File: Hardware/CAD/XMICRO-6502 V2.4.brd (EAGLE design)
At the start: 203.2 x 101.6 mm, 80 parts, among them Q1 2N4403, U1 74138, U10 7474, U11 74273, U12 74244, U13 74244, U14 74244, U15 74245, U16 74574, U17 7400, U18 7408, U19 7404, U2 74138, U20 W65C02S, U21 74244, U22 74138, U23 74148, U24 74244, U25 74244, U26 74273, U27 7432, U28 7432, U29 74257, U3 7400, U30 7474, U31 74LS14N, U4 7404, U5 74257, U6 74688, U7 74688, U8 74244, U9 7474, Y1 4MHz

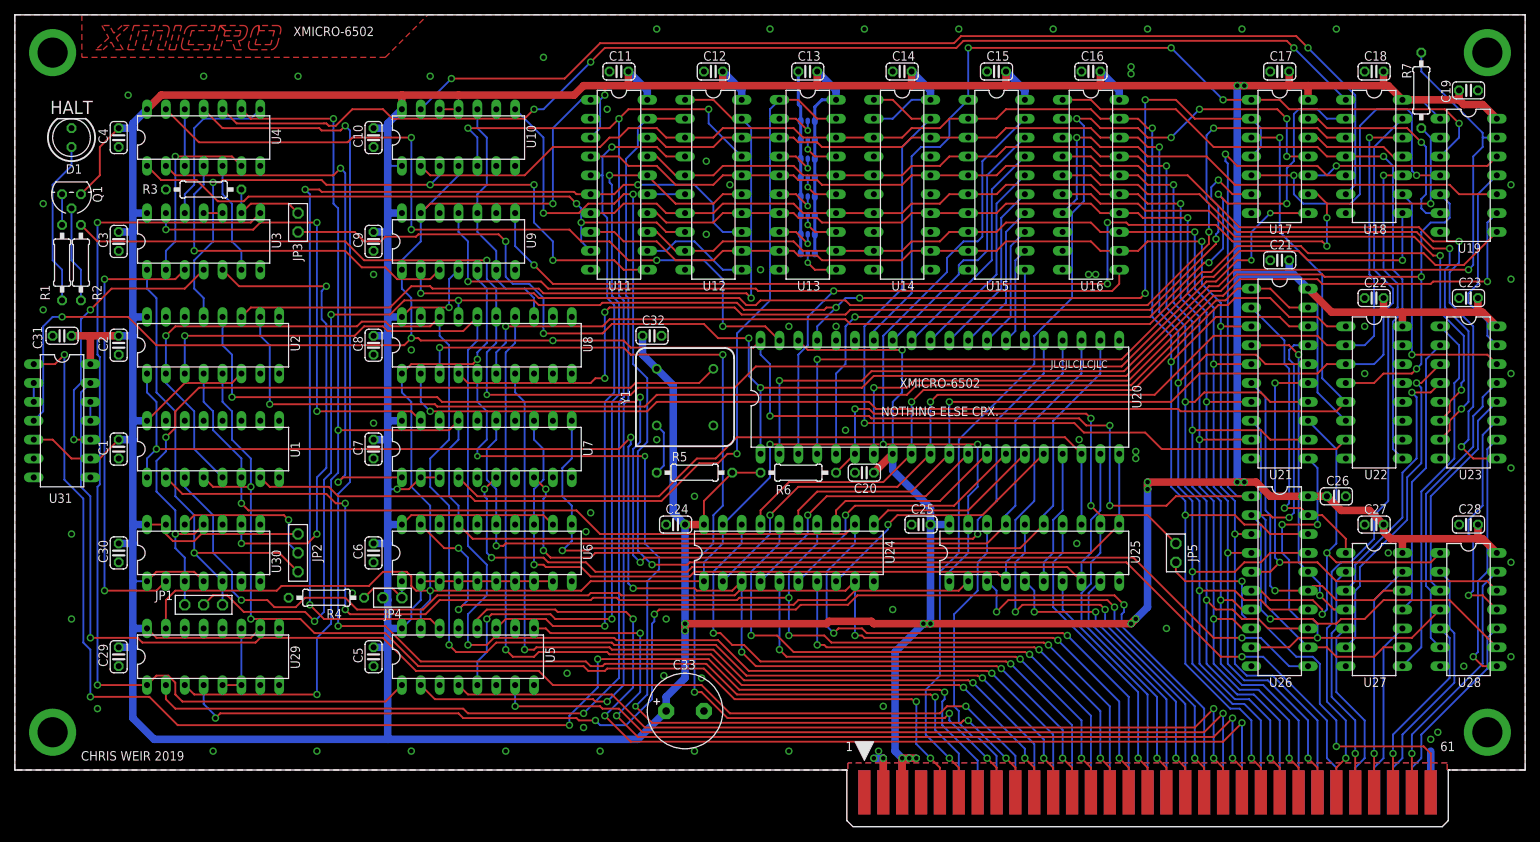
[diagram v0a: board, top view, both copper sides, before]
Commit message: Updated to V2.4 - made it necessary to manually clear DMA interrupts
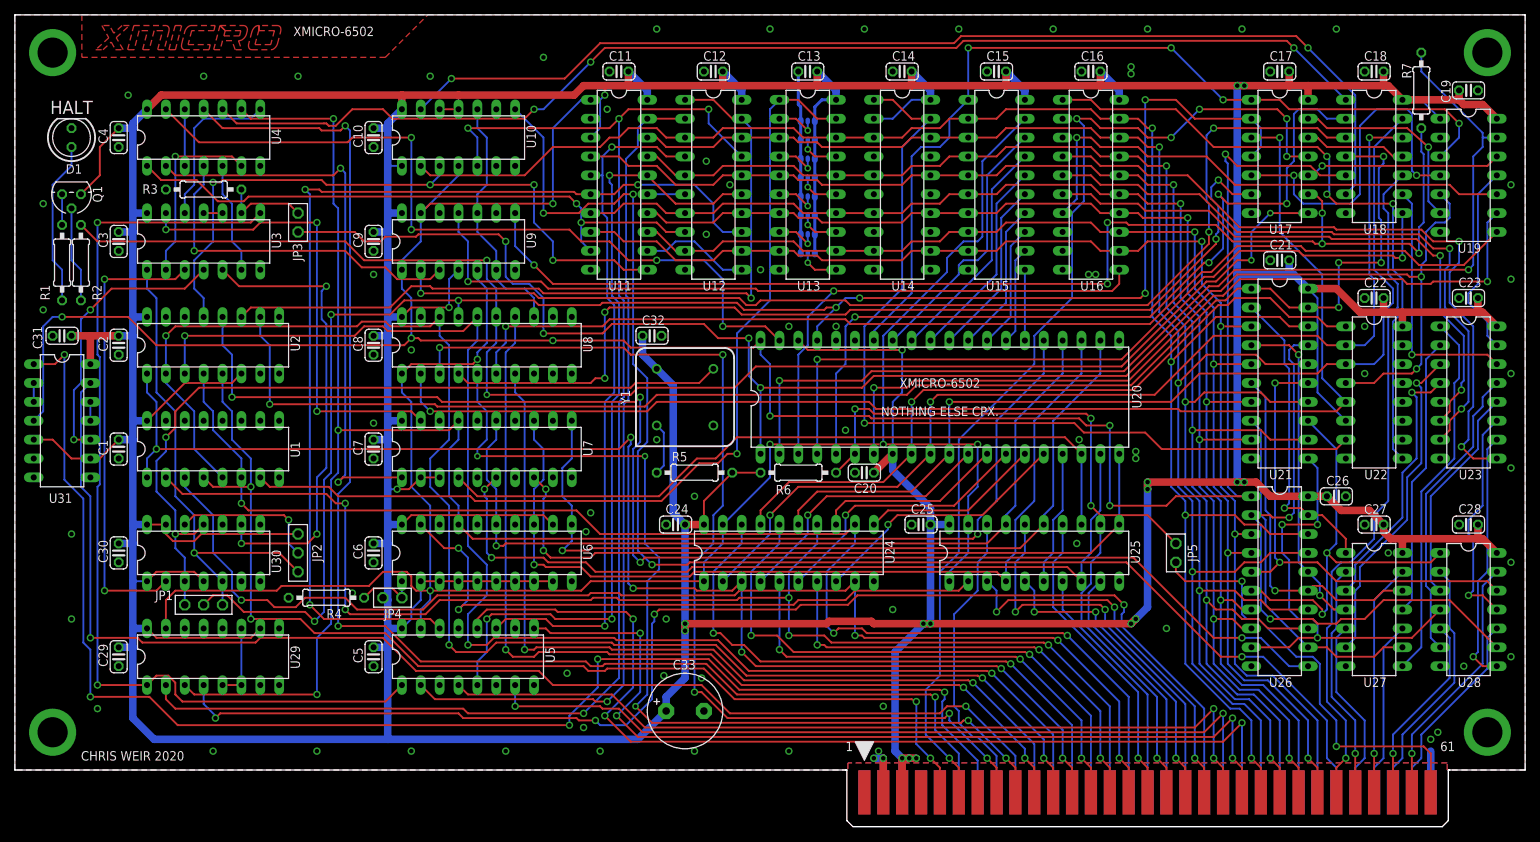
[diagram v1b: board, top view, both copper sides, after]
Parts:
- Y1: value 4MHz -> 12MHz
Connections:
- net !CS1_READ: now also U18.4
- net !IVP: no longer U18.4
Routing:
- net !CS1_READ: track 159.7 -> 195.4 mm, vias 1 -> 5
- net !WAIT_DMA: track 158.8 -> 163.4 mm
- net N$14: track 28.8 -> 27.2 mm
- net !BINT: track 92.6 -> 91.1 mm, vias 2 -> 1
- net !IVP: track 89.1 -> 89.3 mm, vias 1 -> 3
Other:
- board text added: "CHRIS WEIR 2020"
- board text added: "V2.4 2013"
- board text removed: "CHRIS WEIR 2019"
- board text removed: "JLCJLCJLCJLC"
- board text removed: "V2.3 1949"
